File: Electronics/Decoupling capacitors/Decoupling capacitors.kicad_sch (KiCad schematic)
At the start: 32 parts

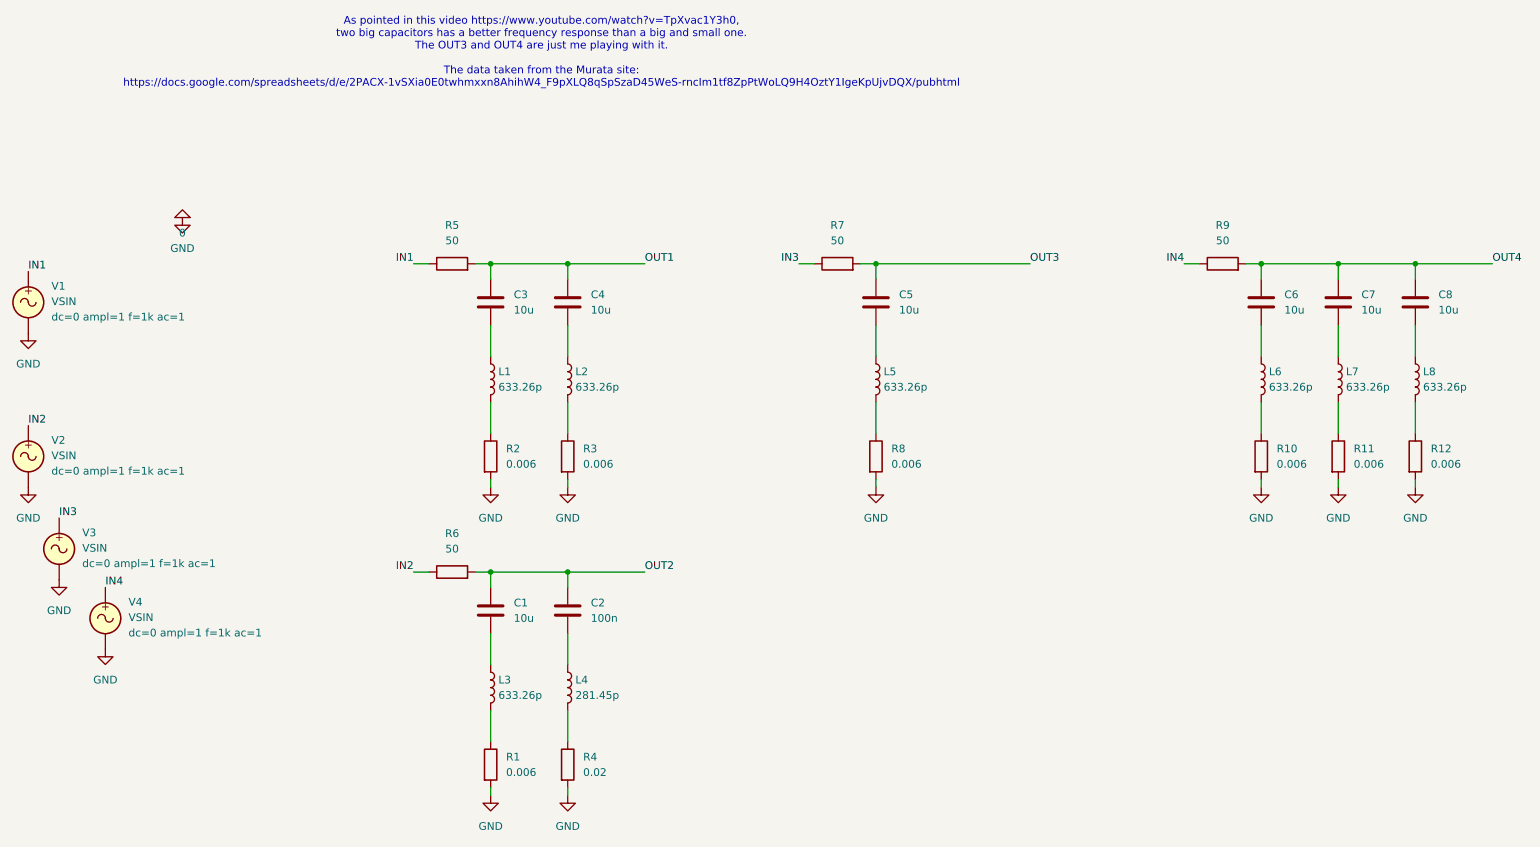
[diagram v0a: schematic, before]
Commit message: Organize decoupling capacitors simulation
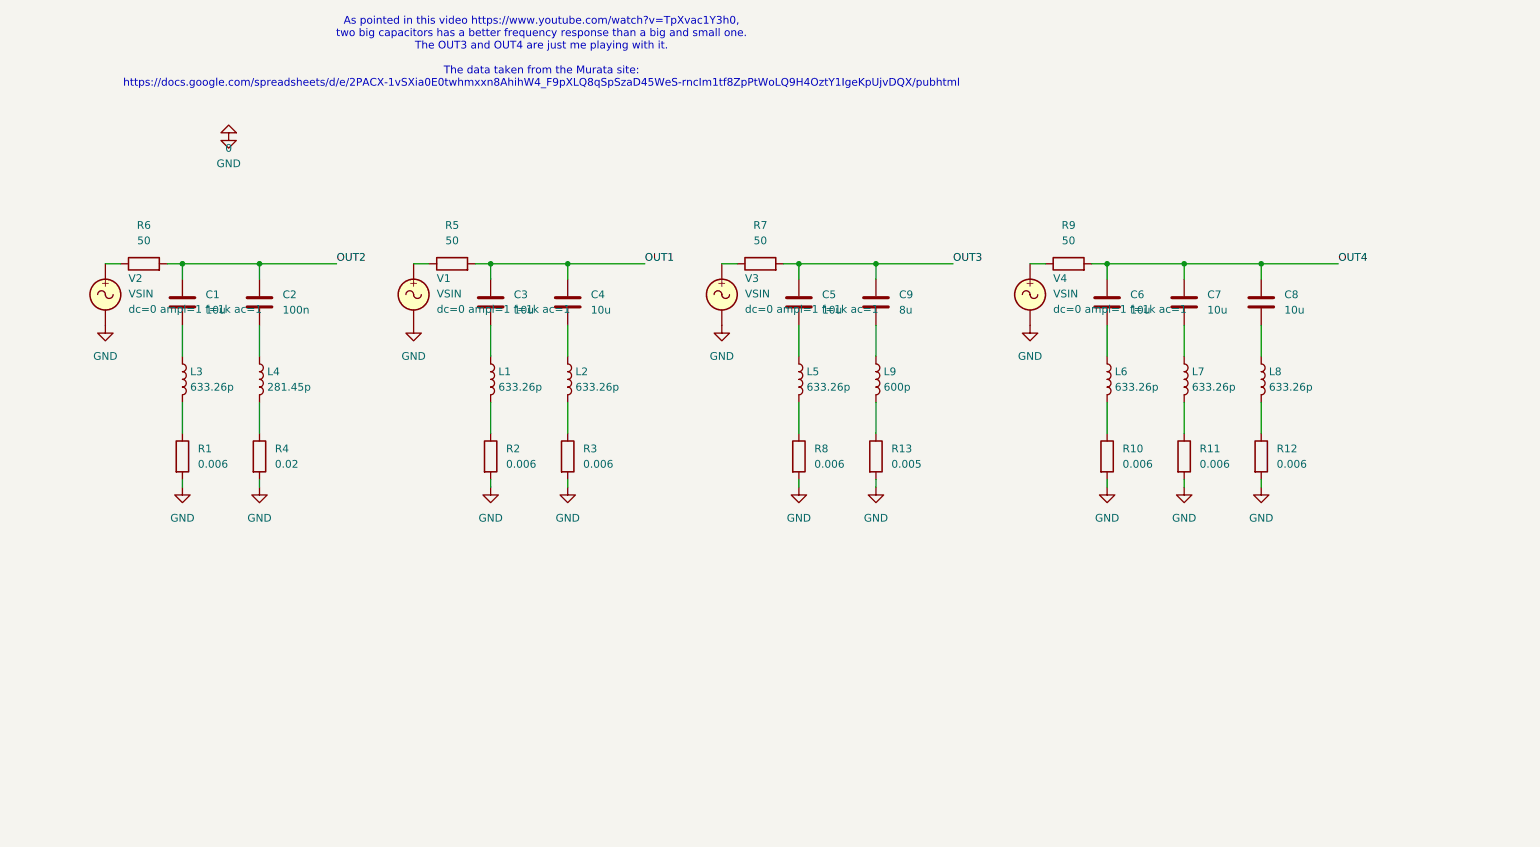
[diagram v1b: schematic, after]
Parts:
- added C9: 8u, symbol Device:C
- added L9: 600p, symbol Device:L
- added R13: 0.005, symbol Device:R
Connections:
- net 0: now also R13.2
- net OUT3: now also C9.1
- net IN1: no longer names the net of R5.1, V1.1
- net IN2: no longer names the net of R6.1, V2.1
- net IN3: no longer names the net of R7.1, V3.1
- net IN4: no longer names the net of R9.1, V4.1
- new net: L9.2, R13.1
- new net: C9.2, L9.1
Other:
- moved on the sheet: C1, C2, C5, C6, C7, C8, L3, L4, L5, L6, L7, L8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
